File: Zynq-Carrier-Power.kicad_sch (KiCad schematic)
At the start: 37 parts, among them J1 Zynq_SoM, J10 Barrel_Jack_MountingPin, J2 B2B-PH-K-S, J3 USB_C_Receptacle_USB2.0_16P, J4 Conn_01x03, J5 Conn_01x03, J6 Conn_01x03, J7 Conn_01x02, J8 Conn_01x02, J9 Conn_01x03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

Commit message: Began work on PCB design for Zynq Carrier
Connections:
- net SW: now reaches C8.1, L1.1, U1.16 (SW)
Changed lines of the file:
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@@
+		)
+	)
+	(label "SYS"
+		(at 358.14 55.88 0)
+		(effects
+			(font
+				(size 1.27 1.27)
+			)
+			(justify left bottom)
 		)
 	)
@@
 		(effects
 			(font
+				(size 1.27 1.27)
+			)
+			(justify left bottom)
+		)
+	)
+	(label "SW"
+		(at 349.25 50.8 0)
+		(effects
+			(font

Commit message: Some errors corrected
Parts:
- removed R5: 100k, Resistor_SMD:R_0603_1608Metric, symbol Device:R_US
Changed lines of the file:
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@@
 	)
 	(junction
-		(at 353.06 121.92)
-		(diameter 0)
-		(color 0 0 0 0)
-	)
-	(junction
 		(at 167.64 109.22)
 		(diameter 0)
@@
 	)
 	(junction
-		(at 353.06 114.3)
-		(diameter 0)
-		(color 0 0 0 0)
-	)
-	(junction
 		(at 13.97 91.44)
 		(diameter 0)
@@
 					(unit 1)
 				)
-			)
-		)
-	)
-	(symbol
-		(lib_name "R_US_1")
-		(lib_id "Device:R_US")
-		(at 353.06 118.11 0)
-		(unit 1)
-		(exclude_from_sim no)
-		(in_bom yes)
-		(on_board yes)
-		(dnp no)
-		(property "Reference" "R5"
-			(at 355.092 115.316 0)
-			(effects
-				(font
-					(size 1.27 1.27)
-				)
-			)
-		)
-		(property "Value" "100k"
-			(at 355.854 120.904 0)
-			(effects
-				(font
-					(size 1.27 1.27)
-				)
-			)
-		)
-		(property "Footprint" "Resistor_SMD:R_0603_1608Metric"
-			(at 354.076 118.364 90)
-			(effects
-				(font
-					(size 1.27 1.27)
-				)
-				(hide yes)
-			)
-		)
-		(property "Datasheet" "~"
-			(at 353.06 118.11 0)
-			(effects
-				(font
-					(size 1.27 1.27)
-				)
-				(hide yes)
-			)
-		)
-		(property "Description" "Resistor, US symbol"
-			(at 353.06 118.11 0)
-			(effects
-				(font
-					(size 1.27 1.27)
-				)
-				(hide yes)
-			)
-		)
-		(pin "2"
-		)
-		(pin "1"
-		)
-		(instances
-			(project "Zynq-Carrier-Template"
-				(path "/e0c786d3-4c71-488f-94d1-904eb052c2b4"
-					(reference "R5")
-					(unit 1)
-				)

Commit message: routed D+D-
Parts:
- removed C5: 10uf, Capacitor_SMD:C_0603_1608Metric, symbol Device:C
- removed C6: 0.1uf, Capacitor_SMD:C_0603_1608Metric, symbol Device:C
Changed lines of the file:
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@@
 	)
 	(junction
-		(at 325.12 30.48)
-		(diameter 0)
-		(color 0 0 0 0)
-	)
-	(junction
 		(at 73.66 60.96)
 		(diameter 0)
@@
 	)
 	(junction
-		(at 325.12 20.32)
-		(diameter 0)
-		(color 0 0 0 0)
-	)
-	(junction
 		(at 13.97 106.68)
 		(diameter 0)
@@
 	)
 	(junction
-		(at 330.2 20.32)
-		(diameter 0)
-		(color 0 0 0 0)
-	)
-	(junction
 		(at 73.66 38.1)
 		(diameter 0)
@@
 	)
 	(junction
-		(at 330.2 30.48)
-		(diameter 0)
-		(color 0 0 0 0)
-	)
-	(junction
 		(at 217.17 123.19)
 		(diameter 0)
@@
 	(wire
 		(pts
-			(xy 330.2 30.48) (xy 325.12 30.48)
-		)
-		(stroke
-			(width 0)
-			(type default)
-		)
-	)
-	(wire
-		(pts
 			(xy 276.86 64.77) (xy 276.86 77.47)
 		)
@@
 	(wire
 		(pts
-			(xy 325.12 30.48) (xy 320.04 30.48)
+			(xy 320.04 30.48) (xy 330.2 30.48)
 		)
 		(stroke
@@
 	(wire
 		(pts
-			(xy 325.12 29.21) (xy 325.12 30.48)
-		)
-		(stroke
-			(width 0)
-			(type default)
-		)
-	)
-	(wire
-		(pts
 			(xy 72.39 30.48) (xy 73.66 30.48)
 		)
@@
 	(wire
 		(pts
-			(xy 335.28 30.48) (xy 330.2 30.48)
-		)
-		(stroke
-			(width 0)
-			(type default)
-		)
-	)
-	(wire
-		(pts
 			(xy 320.04 29.21) (xy 320.04 30.48)
 		)
@@
 	(wire
 		(pts
-			(xy 330.2 20.32) (xy 335.28 20.32)
-		)
-		(stroke
-			(width 0)
-			(type default)
-		)
-	)
-	(wire
-		(pts
 			(xy 349.25 121.92) (xy 353.06 121.92)
 		)
@@
 	(wire
 		(pts
-			(xy 325.12 20.32) (xy 325.12 21.59)
-		)
-		(stroke
-			(width 0)
-			(type default)
-		)
-	)
-	(wire
-		(pts
 			(xy 72.39 38.1) (xy 73.66 38.1)
 		)
@@
 	(wire
 		(pts
-			(xy 335.28 29.21) (xy 335.28 30.48)
-		)
-		(stroke
-			(width 0)
-			(type default)
-		)
-	)
-	(wire
-		(pts
 			(xy 167.64 134.62) (xy 167.64 147.32)
 		)
@@
 	(wire
 		(pts
-			(xy 335.28 20.32) (xy 335.28 21.59)
-		)
-		(stroke
-			(width 0)
-			(type default)
-		)
-	)
-	(wire
-		(pts
 			(xy 166.37 121.92) (xy 167.64 121.92)
 		)
@@
 	(wire
 		(pts
-			(xy 320.04 20.32) (xy 325.12 20.32)
-		)
-		(stroke
-			(width 0)
-			(type default)
-		)
-	)
-	(wire
-		(pts
 			(xy 356.87 50.8) (xy 358.14 50.8)
 		)
@@
 	(wire
 		(pts
-			(xy 325.12 20.32) (xy 330.2 20.32)
+			(xy 320.04 20.32) (xy 330.2 20.32)
 		)
 		(stroke
@@
 	)
 	(symbol
-		(lib_id "Device:C")
-		(at 325.12 25.4 0)
-		(unit 1)
-		(exclude_from_sim no)
-		(in_bom yes)
-		(on_board yes)
-		(dnp no)
-		(property "Reference" "C5"
-			(at 325.628 23.114 0)
-			(effects
-				(font
-					(size 1.27 1.27)
-				)
-				(justify left)
-			)
-		)
-		(property "Value" "10uf"
-			(at 325.628 27.94 0)
-			(effects
-				(font
-					(size 1.27 1.27)
-				)
-				(justify left)
-			)
-		)
-		(property "Footprint" "Capacitor_SMD:C_0603_1608Metric"
-			(at 326.0852 29.21 0)
-			(effects
-				(font
-					(size 1.27 1.27)
-				)
-				(hide yes)
-			)
-		)
-		(property "Datasheet" "~"
-			(at 325.12 25.4 0)
-			(effects
-				(font
-					(size 1.27 1.27)
-				)
-				(hide yes)
-			)
-		)
-		(property "Description" "Unpolarized capacitor"
-			(at 325.12 25.4 0)
-			(effects
-				(font
-					(size 1.27 1.27)
-				)
-				(hide yes)
-			)
-		)
-		(pin "2"
-		)
-		(pin "1"
-		)
-		(instances
-			(project "Zynq-Carrier-Template"
-				(path "/e0c786d3-4c71-488f-94d1-904eb052c2b4"
-					(reference "C5")
-					(unit 1)
-				)
-			)
-		)
-	)
-	(symbol
 		(lib_id "JST_Pins:B2B-PH-K-S")
 		(at 370.84 46.99 270)
@@
 					(unit 1)
 				)
-			)
-		)
-	)
-	(symbol
-		(lib_id "Device:C")
-		(at 335.28 25.4 0)
-		(unit 1)
-		(exclude_from_sim no)
-		(in_bom yes)
-		(on_board yes)
-		(dnp no)
-		(property "Reference" "C6"
-			(at 335.534 23.114 0)
-			(effects
-				(font
-					(size 1.27 1.27)
-				)
-				(justify left)
-			)
-		)
-		(property "Value" "0.1uf"
-			(at 335.788 27.94 0)
-			(effects
-				(font
-					(size 1.27 1.27)
-				)
-				(justify left)
-			)
-		)
-		(property "Footprint" "Capacitor_SMD:C_0603_1608Metric"
-			(at 336.2452 29.21 0)
-			(effects
-				(font
-					(size 1.27 1.27)
-				)
-				(hide yes)
-			)
-		)
-		(property "Datasheet" "~"
-			(at 335.28 25.4 0)
-			(effects
-				(font
-					(size 1.27 1.27)
-				)
-				(hide yes)
-			)
-		)
-		(property "Description" "Unpolarized capacitor"
-			(at 335.28 25.4 0)
-			(effects
-				(font
-					(size 1.27 1.27)
-				)
-				(hide yes)
-			)
-		)
-		(pin "2"
-		)
-		(pin "1"
-		)
-		(instances
-			(project "Zynq-Carrier-Template"
-				(path "/e0c786d3-4c71-488f-94d1-904eb052c2b4"
-					(reference "C6")
-					(unit 1)
-				)

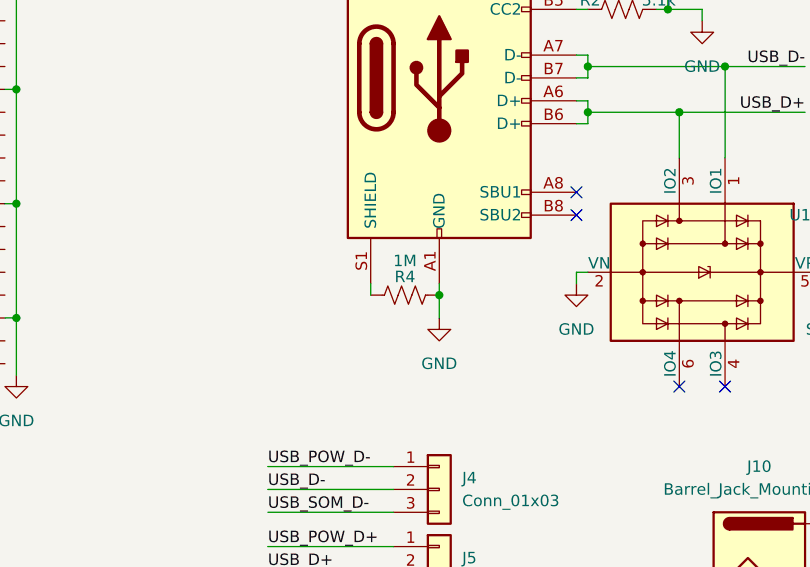
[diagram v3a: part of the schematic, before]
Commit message: Modified PCB & Schematic for new constraints
Modifications are not done yet. Some errors are still present
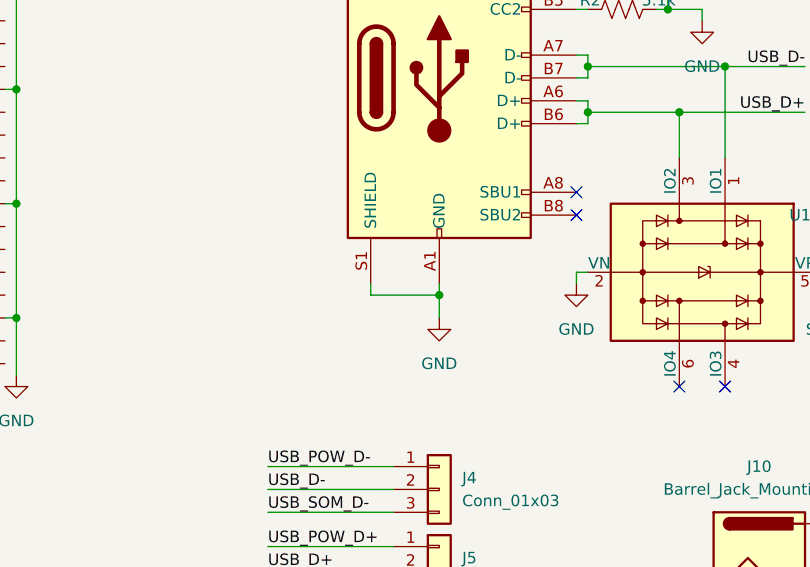
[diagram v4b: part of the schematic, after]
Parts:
- removed R4: 1M, Resistor_SMD:R_0603_1608Metric, symbol Device:R_US
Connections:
- net GND: now also J3.S1 (SHIELD)
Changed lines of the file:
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@@
 	)
 	(junction
+		(at 323.85 153.67)
+		(diameter 0)
+		(color 0 0 0 0)
+	)
+	(junction
 		(at 13.97 106.68)
 		(diameter 0)
@@
 	)
 	(junction
-		(at 323.85 153.67)
-		(diameter 0)
-		(color 0 0 0 0)
-	)
-	(junction
 		(at 13.97 55.88)
 		(diameter 0)
@@
 	(wire
 		(pts
+			(xy 323.85 153.67) (xy 323.85 156.21)
+		)
+		(stroke
+			(width 0)
+			(type default)
+		)
+	)
+	(wire
+		(pts
 			(xy 339.09 152.4) (xy 339.09 151.13)
 		)
@@
 	(wire
 		(pts
+			(xy 316.23 153.67) (xy 323.85 153.67)
+		)
+		(stroke
+			(width 0)
+			(type default)
+		)
+	)
+	(wire
+		(pts
 			(xy 218.44 97.79) (xy 217.17 97.79)
 		)
@@
 	(wire
 		(pts
-			(xy 323.85 156.21) (xy 323.85 153.67)
-		)
-		(stroke
-			(width 0)
-			(type default)
-		)
-	)
-	(wire
-		(pts
 			(xy 275.59 90.17) (xy 276.86 90.17)
 		)
@@
 					(unit 1)
 				)
-			)
-		)
-	)
-	(symbol
-		(lib_id "Device:R_US")
-		(at 320.04 153.67 90)
-		(unit 1)
-		(exclude_from_sim no)
-		(in_bom yes)
-		(on_board yes)
-		(dnp no)
-		(property "Reference" "R4"
-			(at 320.04 151.638 90)
-			(effects
-				(font
-					(size 1.27 1.27)
-				)
-			)
-		)
-		(property "Value" "1M"
-			(at 320.04 149.86 90)
-			(effects
-				(font
-					(size 1.27 1.27)
-				)
-			)
-		)
-		(property "Footprint" "Resistor_SMD:R_0603_1608Metric"
-			(at 320.294 152.654 90)
-			(effects
-				(font
-					(size 1.27 1.27)
-				)
-				(hide yes)
-			)
-		)
-		(property "Datasheet" "~"
-			(at 320.04 153.67 0)
-			(effects
-				(font
-					(size 1.27 1.27)
-				)
-				(hide yes)
-			)
-		)
-		(property "Description" "Resistor, US symbol"
-			(at 320.04 153.67 0)
-			(effects
-				(font
-					(size 1.27 1.27)
-				)
-				(hide yes)
-			)
-		)
-		(pin "2"
-		)
-		(pin "1"
-		)
-		(instances
-			(project "Zynq-Carrier-Template"
-				(path "/e0c786d3-4c71-488f-94d1-904eb052c2b4"
-					(reference "R4")
-					(unit 1)
-				)
